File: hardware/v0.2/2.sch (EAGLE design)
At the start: 36 parts, among them IC1 STM32F10XCXT6, IC2 ADXL345"

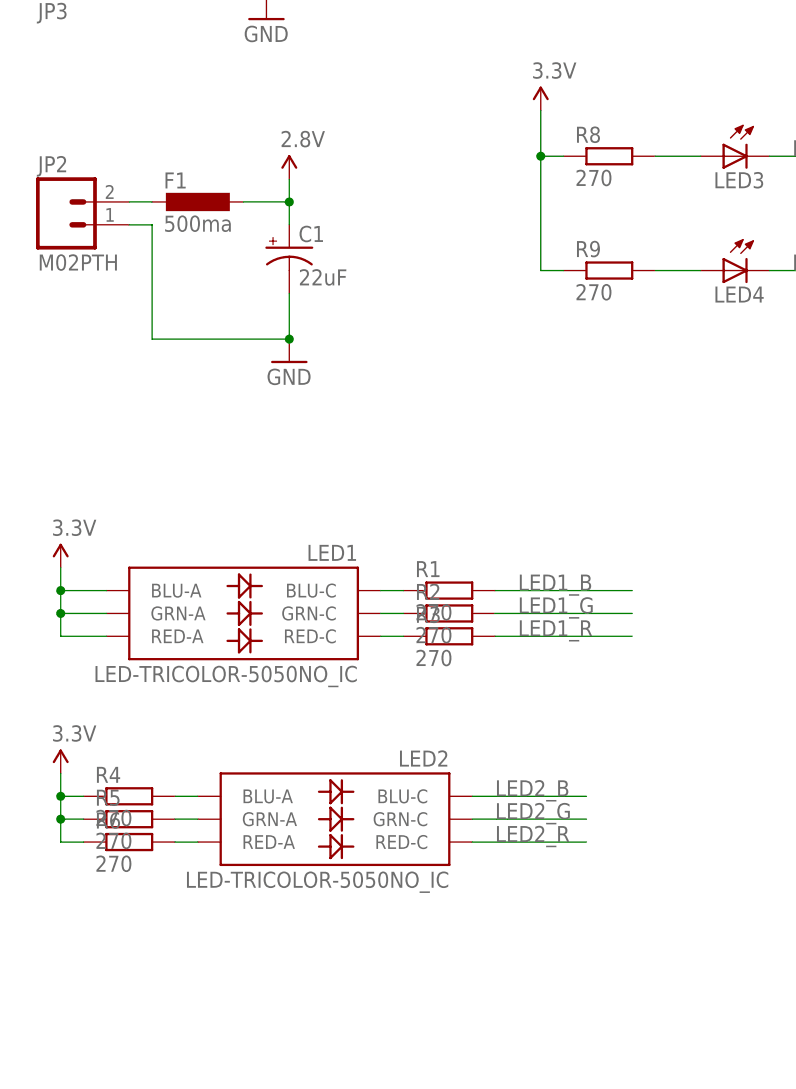
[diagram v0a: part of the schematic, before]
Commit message: update schematic for clearance
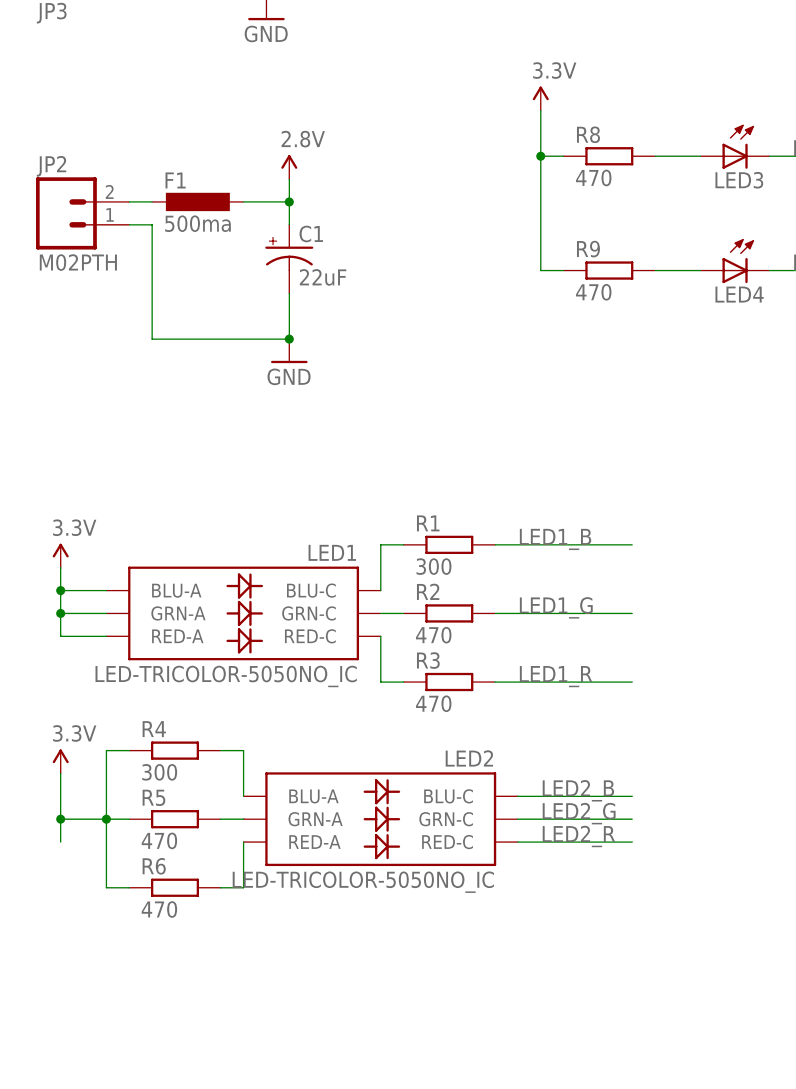
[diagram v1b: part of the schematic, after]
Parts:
- R1, R4: value 270 -> 300
- R2, R3, R5, R6, R8, R9: value 270 -> 470
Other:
- moved on the sheet: LED2, R1, R3, R4, R5, R6
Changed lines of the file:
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@@
 <part name="LED3" library="SparkFun-LED" deviceset="LED" device="1206"/>
 <part name="LED4" library="SparkFun-LED" deviceset="LED" device="1206"/>
-<part name="R8" library="rcl" deviceset="R-EU_" device="R0603" value="270"/>
-<part name="R9" library="rcl" deviceset="R-EU_" device="R0603" value="270"/>
+<part name="R8" library="rcl" deviceset="R-EU_" device="R0603" value="470"/>
+<part name="R9" library="rcl" deviceset="R-EU_" device="R0603" value="470"/>
 <part name="IC3" library="digital-toy" deviceset="BL8530-XX2_RN" device=""/>
 <part name="C5" library="SparkFun-Capacitors" deviceset="47UF-TANT" device="" value="100uF"/>
 <part name="SUPPLY10" library="SparkFun-Aesthetics" deviceset="2.8V" device=""/>
-<part name="R1" library="rcl" deviceset="R-EU_" device="R0603" value="270"/>
-<part name="R2" library="rcl" deviceset="R-EU_" device="R0603" value="270"/>
-<part name="R3" library="rcl" deviceset="R-EU_" device="R0603" value="270"/>
-<part name="R4" library="rcl" deviceset="R-EU_" device="R0603" value="270"/>
-<part name="R5" library="rcl" deviceset="R-EU_" device="R0603" value="270"/>
-<part name="R6" library="rcl" deviceset="R-EU_" device="R0603" value="270"/>
+<part name="R1" library="rcl" deviceset="R-EU_" device="R0603" value="300"/>
+<part name="R2" library="rcl" deviceset="R-EU_" device="R0603" value="470"/>
+<part name="R3" library="rcl" deviceset="R-EU_" device="R0603" value="470"/>
+<part name="R4" library="rcl" deviceset="R-EU_" device="R0603" value="300"/>
+<part name="R5" library="rcl" deviceset="R-EU_" device="R0603" value="470"/>
+<part name="R6" library="rcl" deviceset="R-EU_" device="R0603" value="470"/>
 <part name="SUPPLY2" library="SparkFun-Aesthetics" deviceset="3.3V" device=""/>
 <part name="SUPPLY11" library="SparkFun-Aesthetics" deviceset="2.8V" device=""/>
@@
 </instance>
 <instance part="LED1" gate="D1" x="10.16" y="-27.94" rot="MR0"/>
-<instance part="LED2" gate="D1" x="20.32" y="-50.8" rot="MR0"/>
+<instance part="LED2" gate="D1" x="25.4" y="-50.8" rot="MR0"/>
 <instance part="LED3" gate="G$1" x="63.5" y="22.86" rot="MR270"/>
 <instance part="LED4" gate="G$1" x="63.5" y="10.16" rot="MR270"/>
@@
 <instance part="C5" gate="G$1" x="144.78" y="-71.12"/>
 <instance part="SUPPLY10" gate="G$1" x="15.24" y="20.32"/>
-<instance part="R1" gate="G$1" x="33.02" y="-25.4"/>
+<instance part="R1" gate="G$1" x="33.02" y="-20.32"/>
 <instance part="R2" gate="G$1" x="33.02" y="-27.94"/>
-<instance part="R3" gate="G$1" x="33.02" y="-30.48"/>
-<instance part="R4" gate="G$1" x="-2.54" y="-48.26"/>
-<instance part="R5" gate="G$1" x="-2.54" y="-50.8"/>
-<instance part="R6" gate="G$1" x="-2.54" y="-53.34"/>
+<instance part="R3" gate="G$1" x="33.02" y="-35.56"/>
+<instance part="R4" gate="G$1" x="2.54" y="-43.18"/>
+<instance part="R5" gate="G$1" x="2.54" y="-50.8"/>
+<instance part="R6" gate="G$1" x="2.54" y="-58.42"/>
 <instance part="SUPPLY2" gate="G$1" x="144.78" y="-53.34"/>
 <instance part="SUPPLY11" gate="G$1" x="12.7" y="55.88"/>
@@
 </segment>
 </net>
-<net name="N$9" class="0">
-<segment>
-<pinref part="R4" gate="G$1" pin="2"/>
-<pinref part="LED2" gate="D1" pin="BLU-A"/>
-<wire x1="2.54" y1="-48.26" x2="5.08" y2="-48.26" width="0.1524" layer="91"/>
-</segment>
-</net>
 <net name="N$10" class="0">
 <segment>
 <pinref part="R5" gate="G$1" pin="2"/>
 <pinref part="LED2" gate="D1" pin="GRN-A"/>
-<wire x1="2.54" y1="-50.8" x2="5.08" y2="-50.8" width="0.1524" layer="91"/>
-</segment>
-</net>
-<net name="N$11" class="0">
-<segment>
-<pinref part="R6" gate="G$1" pin="2"/>
-<pinref part="LED2" gate="D1" pin="RED-A"/>
-<wire x1="2.54" y1="-53.34" x2="5.08" y2="-53.34" width="0.1524" layer="91"/>
+<wire x1="7.62" y1="-50.8" x2="10.16" y2="-50.8" width="0.1524" layer="91"/>
 </segment>
 </net>
@@
 <segment>
 <pinref part="SUPPLY3" gate="G$1" pin="3.3V"/>
-<wire x1="-10.16" y1="-45.72" x2="-10.16" y2="-48.26" width="0.1524" layer="91"/>
-<pinref part="R6" gate="G$1" pin="1"/>
-<wire x1="-10.16" y1="-48.26" x2="-10.16" y2="-50.8" width="0.1524" layer="91"/>
+<wire x1="-10.16" y1="-45.72" x2="-10.16" y2="-50.8" width="0.1524" layer="91"/>
 <wire x1="-10.16" y1="-50.8" x2="-10.16" y2="-53.34" width="0.1524" layer="91"/>
-<wire x1="-10.16" y1="-53.34" x2="-7.62" y2="-53.34" width="0.1524" layer="91"/>
 <pinref part="R5" gate="G$1" pin="1"/>
-<wire x1="-7.62" y1="-50.8" x2="-10.16" y2="-50.8" width="0.1524" layer="91"/>
+<wire x1="-2.54" y1="-50.8" x2="-5.08" y2="-50.8" width="0.1524" layer="91"/>
 <junction x="-10.16" y="-50.8"/>
 <pinref part="R4" gate="G$1" pin="1"/>
-<wire x1="-7.62" y1="-48.26" x2="-10.16" y2="-48.26" width="0.1524" layer="91"/>
-<junction x="-10.16" y="-48.26"/>
+<wire x1="-5.08" y1="-50.8" x2="-10.16" y2="-50.8" width="0.1524" layer="91"/>
+<wire x1="-2.54" y1="-43.18" x2="-5.08" y2="-43.18" width="0.1524" layer="91"/>
+<wire x1="-5.08" y1="-43.18" x2="-5.08" y2="-50.8" width="0.1524" layer="91"/>
+<junction x="-5.08" y="-50.8"/>
+<pinref part="R6" gate="G$1" pin="1"/>
+<wire x1="-2.54" y1="-58.42" x2="-5.08" y2="-58.42" width="0.1524" layer="91"/>
+<wire x1="-5.08" y1="-58.42" x2="-5.08" y2="-50.8" width="0.1524" layer="91"/>
 </segment>
 <segment>
@@
 <segment>
 <pinref part="LED2" gate="D1" pin="BLU-C"/>
-<wire x1="35.56" y1="-48.26" x2="48.26" y2="-48.26" width="0.1524" layer="91"/>
-<label x="38.1" y="-48.26" size="1.778" layer="95"/>
+<wire x1="40.64" y1="-48.26" x2="53.34" y2="-48.26" width="0.1524" layer="91"/>
+<label x="43.18" y="-48.26" size="1.778" layer="95"/>
 </segment>
 <segment>
@@
 <segment>
 <pinref part="LED2" gate="D1" pin="GRN-C"/>
-<wire x1="35.56" y1="-50.8" x2="48.26" y2="-50.8" width="0.1524" layer="91"/>
-<label x="38.1" y="-50.8" size="1.778" layer="95"/>
+<wire x1="40.64" y1="-50.8" x2="53.34" y2="-50.8" width="0.1524" layer="91"/>
+<label x="43.18" y="-50.8" size="1.778" layer="95"/>
 </segment>
 <segment>
@@
 <segment>
 <pinref part="LED2" gate="D1" pin="RED-C"/>
-<wire x1="35.56" y1="-53.34" x2="48.26" y2="-53.34" width="0.1524" layer="91"/>
-<label x="38.1" y="-53.34" size="1.778" layer="95"/>
+<wire x1="40.64" y1="-53.34" x2="53.34" y2="-53.34" width="0.1524" layer="91"/>
+<label x="43.18" y="-53.34" size="1.778" layer="95"/>
 </segment>
 <segment>
@@
 </segment>
 </net>
-<net name="N$6" class="0">
-<segment>
-<pinref part="R1" gate="G$1" pin="1"/>
-<pinref part="LED1" gate="D1" pin="BLU-C"/>
-<wire x1="27.94" y1="-25.4" x2="25.4" y2="-25.4" width="0.1524" layer="91"/>
-</segment>
-</net>
 <net name="N$7" class="0">
 <segment>
@@
 </segment>
 </net>
-<net name="N$8" class="0">
-<segment>
-<pinref part="R3" gate="G$1" pin="1"/>
-<pinref part="LED1" gate="D1" pin="RED-C"/>
-<wire x1="27.94" y1="-30.48" x2="25.4" y2="-30.48" width="0.1524" layer="91"/>
-</segment>
-</net>
 <net name="LED1_G" class="0">
 <segment>
@@
 <segment>
 <pinref part="R3" gate="G$1" pin="2"/>
-<wire x1="38.1" y1="-30.48" x2="53.34" y2="-30.48" width="0.1524" layer="91"/>
-<label x="40.64" y="-30.48" size="1.778" layer="95"/>
+<wire x1="38.1" y1="-35.56" x2="53.34" y2="-35.56" width="0.1524" layer="91"/>
+<label x="40.64" y="-35.56" size="1.778" layer="95"/>
 </segment>
 <segment>
@@
 <segment>
 <pinref part="R1" gate="G$1" pin="2"/>
-<wire x1="38.1" y1="-25.4" x2="53.34" y2="-25.4" width="0.1524" layer="91"/>
-<label x="40.64" y="-25.4" size="1.778" layer="95"/>
+<wire x1="38.1" y1="-20.32" x2="53.34" y2="-20.32" width="0.1524" layer="91"/>
+<label x="40.64" y="-20.32" size="1.778" layer="95"/>
 </segment>
 </net>
@@
 </segment>
 </net>
+<net name="N$6" class="0">
+<segment>
+<pinref part="R4" gate="G$1" pin="2"/>
+<pinref part="LED2" gate="D1" pin="BLU-A"/>
+<wire x1="7.62" y1="-43.18" x2="10.16" y2="-43.18" width="0.1524" layer="91"/>
+<wire x1="10.16" y1="-43.18" x2="10.16" y2="-48.26" width="0.1524" layer="91"/>
+</segment>
+</net>
+<net name="N$8" class="0">
+<segment>
+<pinref part="LED2" gate="D1" pin="RED-A"/>
+<wire x1="10.16" y1="-53.34" x2="10.16" y2="-58.42" width="0.1524" layer="91"/>
+<pinref part="R6" gate="G$1" pin="2"/>
+<wire x1="10.16" y1="-58.42" x2="7.62" y2="-58.42" width="0.1524" layer="91"/>
+</segment>
+</net>
+<net name="N$9" class="0">
+<segment>
+<pinref part="R1" gate="G$1" pin="1"/>
+<pinref part="LED1" gate="D1" pin="BLU-C"/>
+<wire x1="27.94" y1="-20.32" x2="25.4" y2="-20.32" width="0.1524" layer="91"/>
+<wire x1="25.4" y1="-20.32" x2="25.4" y2="-25.4" width="0.1524" layer="91"/>
+</segment>
+</net>
+<net name="N$11" class="0">
+<segment>
+<pinref part="LED1" gate="D1" pin="RED-C"/>
+<wire x1="25.4" y1="-30.48" x2="25.4" y2="-35.56" width="0.1524" layer="91"/>
+<pinref part="R3" gate="G$1" pin="1"/>
+<wire x1="25.4" y1="-35.56" x2="27.94" y2="-35.56" width="0.1524" layer="91"/>
+</segment>
+</net>
